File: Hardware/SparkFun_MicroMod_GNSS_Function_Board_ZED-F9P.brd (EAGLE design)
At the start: 37.5 x 65 mm, 160 parts, among them J1 USB Female Type C Connector, J10 U.FL, J11 455-1750-1-ND, J2 MICROMOD_FUNCTION_STANDARD, Q1 DMP21D0UT-7, U1 NLAST4501DFT2G, U10 SN74AUP1T04, U11 SN74AUP1T04, U2 3.3V, U3 EEPROM, U4 74LVC4066D_QUAD_BILATERAL_SWI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, U5 74LVC4066D_QUAD_BILATERAL_SWI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, U6 OPA344, U7 74LVC541A, U8 U-BLOX_ZED-F9P, U9 FIN1017MX

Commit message: Removed Acid Traps.
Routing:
- net ZED_DSEL: track 41.1 -> 41.5 mm, vias 6 -> 5
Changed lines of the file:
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@@
 <layer number="1" name="Top/Horz" color="4" fill="1" visible="yes" active="yes"/>
 <layer number="2" name="Route2" color="13" fill="3" visible="yes" active="yes"/>
-<layer number="15" name="Route15" color="47" fill="6" visible="yes" active="yes"/>
-<layer number="16" name="Bottom/Vert" color="9" fill="1" visible="yes" active="yes"/>
+<layer number="15" name="Route15" color="47" fill="6" visible="no" active="yes"/>
+<layer number="16" name="Bottom/Vert" color="9" fill="1" visible="no" active="yes"/>
 <layer number="17" name="Pads" color="2" fill="1" visible="yes" active="yes"/>
 <layer number="18" name="Vias" color="2" fill="1" visible="yes" active="yes"/>
-<layer number="19" name="Unrouted" color="6" fill="1" visible="yes" active="yes"/>
+<layer number="19" name="Unrouted" color="6" fill="1" visible="no" active="yes"/>
 <layer number="20" name="Dimension" color="24" fill="1" visible="yes" active="yes"/>
-<layer number="21" name="tPlace" color="16" fill="1" visible="yes" active="yes"/>
-<layer number="22" name="bPlace" color="14" fill="1" visible="yes" active="yes"/>
-<layer number="23" name="tOrigins" color="15" fill="1" visible="yes" active="yes"/>
-<layer number="24" name="bOrigins" color="15" fill="1" visible="yes" active="yes"/>
+<layer number="21" name="tPlace" color="16" fill="1" visible="no" active="yes"/>
+<layer number="22" name="bPlace" color="14" fill="1" visible="no" active="yes"/>
+<layer number="23" name="tOrigins" color="15" fill="1" visible="no" active="yes"/>
+<layer number="24" name="bOrigins" color="15" fill="1" visible="no" active="yes"/>
 <layer number="25" name="tNames" color="7" fill="1" visible="no" active="yes"/>
 <layer number="26" name="bNames" color="7" fill="1" visible="no" active="yes"/>
@@
 <layer number="37" name="tTest" color="7" fill="1" visible="no" active="yes"/>
 <layer number="38" name="bTest" color="7" fill="1" visible="no" active="yes"/>
-<layer number="39" name="tKeepout" color="4" fill="11" visible="yes" active="yes"/>
-<layer number="40" name="bKeepout" color="1" fill="11" visible="yes" active="yes"/>
-<layer number="41" name="tRestrict" color="4" fill="10" visible="yes" active="yes"/>
-<layer number="42" name="bRestrict" color="1" fill="10" visible="yes" active="yes"/>
+<layer number="39" name="tKeepout" color="4" fill="11" visible="no" active="yes"/>
+<layer number="40" name="bKeepout" color="1" fill="11" visible="no" active="yes"/>
+<layer number="41" name="tRestrict" color="4" fill="10" visible="no" active="yes"/>
+<layer number="42" name="bRestrict" color="1" fill="10" visible="no" active="yes"/>
 <layer number="43" name="vRestrict" color="2" fill="10" visible="no" active="yes"/>
 <layer number="44" name="Drills" color="7" fill="1" visible="no" active="yes"/>
-<layer number="45" name="Holes" color="7" fill="1" visible="yes" active="yes"/>
-<layer number="46" name="Milling" color="3" fill="1" visible="yes" active="yes"/>
-<layer number="47" name="Measures" color="7" fill="1" visible="yes" active="yes"/>
-<layer number="48" name="Document" color="7" fill="1" visible="yes" active="yes"/>
+<layer number="45" name="Holes" color="7" fill="1" visible="no" active="yes"/>
+<layer number="46" name="Milling" color="3" fill="1" visible="no" active="yes"/>
+<layer number="47" name="Measures" color="7" fill="1" visible="no" active="yes"/>
+<layer number="48" name="Document" color="7" fill="1" visible="no" active="yes"/>
 <layer number="49" name="Reference" color="7" fill="1" visible="no" active="yes"/>
 <layer number="50" name="dxf" color="7" fill="1" visible="no" active="yes"/>
-<layer number="51" name="tDocu" color="6" fill="1" visible="yes" active="yes"/>
-<layer number="52" name="bDocu" color="7" fill="1" visible="yes" active="yes"/>
+<layer number="51" name="tDocu" color="6" fill="1" visible="no" active="yes"/>
+<layer number="52" name="bDocu" color="7" fill="1" visible="no" active="yes"/>
 <layer number="91" name="Nets" color="2" fill="1" visible="no" active="no"/>
 <layer number="92" name="Busses" color="1" fill="1" visible="no" active="no"/>
@@
 <wire x1="17.865" y1="24.235" x2="16.695" y2="25.405" width="0.2" layer="2"/>
 <wire x1="17.865" y1="26.4" x2="17.865" y2="24.135" width="0.2" layer="1"/>
-<wire x1="20.405" y1="20.8" x2="20.405" y2="22.005" width="0.2" layer="1"/>
-<wire x1="21.675" y1="23.275" x2="20.405" y2="22.005" width="0.2" layer="2"/>
 <wire x1="21.675" y1="23.275" x2="21.7" y2="23.3" width="0.2" layer="2"/>
 <wire x1="21.675" y1="20.8" x2="21.675" y2="23.275" width="0.2" layer="1"/>
@@
 <via x="16.695" y="25.405" extent="1-16" drill="0.3"/>
 <via x="23.7" y="28.8" extent="1-16" drill="0.3"/>
-<via x="20.405" y="22.005" extent="1-16" drill="0.3"/>
 <via x="21.675" y="23.275" extent="1-16" drill="0.3"/>
 <wire x1="24.95" y1="42.2" x2="26.1" y2="42.2" width="0.11" layer="1"/>
@@
 <wire x1="24.4" y1="27.4" x2="23.7" y2="28.1" width="0.11" layer="16"/>
 <wire x1="23.7" y1="28.1" x2="23.7" y2="28.8" width="0.11" layer="16"/>
+<wire x1="20.405" y1="20.8" x2="20.405" y2="22.605" width="0.2" layer="1"/>
+<wire x1="20.405" y1="22.605" x2="21.1" y2="23.3" width="0.2" layer="1"/>
+<wire x1="21.1" y1="23.3" x2="21.65" y2="23.3" width="0.2" layer="1"/>
+<wire x1="21.65" y1="23.3" x2="21.675" y2="23.275" width="0.2" layer="1"/>
 </signal>
 <signal name="ZED_ANT_DETECT" class="11">
@@
 <contactref element="U5" pad="6"/>
 <contactref element="U5" pad="12"/>
-<wire x1="5.765" y1="24.135" x2="6.8" y2="23.1" width="0.2" layer="2"/>
+<wire x1="5.765" y1="24.135" x2="6.3" y2="23.6" width="0.2" layer="2"/>
 <wire x1="5.765" y1="24.135" x2="4.495" y2="25.405" width="0.2" layer="2"/>
 <wire x1="4.495" y1="25.405" x2="4.495" y2="26.4" width="0.2" layer="1"/>
@@
 <wire x1="16.05" y1="29.45" x2="15.95" y2="29.45" width="0.2" layer="15"/>
 <wire x1="15.95" y1="29.45" x2="9.6" y2="23.1" width="0.2" layer="15"/>
-<wire x1="6.8" y1="23.1" x2="9.6" y2="23.1" width="0.2" layer="2"/>
+<wire x1="9.1" y1="23.6" x2="6.3" y2="23.6" width="0.2" layer="2"/>
+<wire x1="9.1" y1="23.6" x2="9.6" y2="23.1" width="0.2" layer="2"/>
 <wire x1="9.6" y1="23.1" x2="9.6" y2="20.825" width="0.2" layer="1"/>
 <wire x1="9.6" y1="20.825" x2="9.575" y2="20.8" width="0.2" layer="1"/>

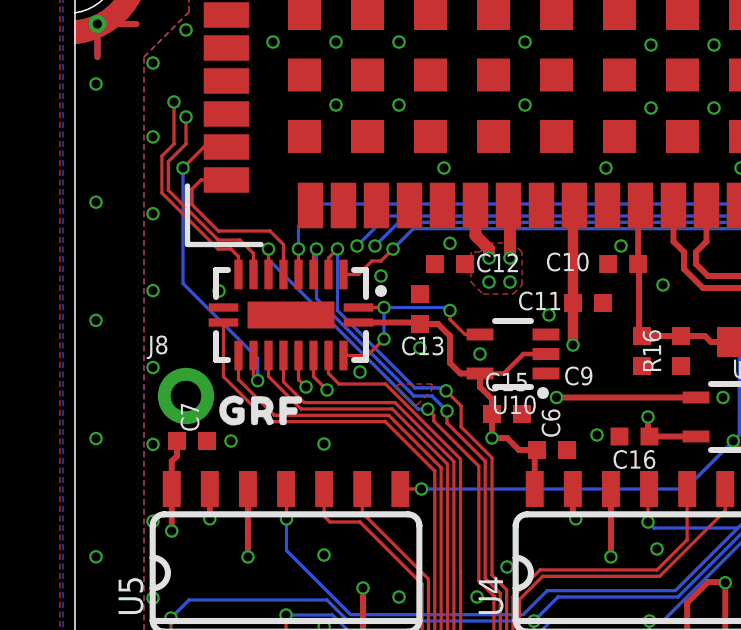
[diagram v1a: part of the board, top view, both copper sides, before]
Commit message: change due to mfgring issue.
There was no TSTOP on ground pad of U7. Added TSTOP.
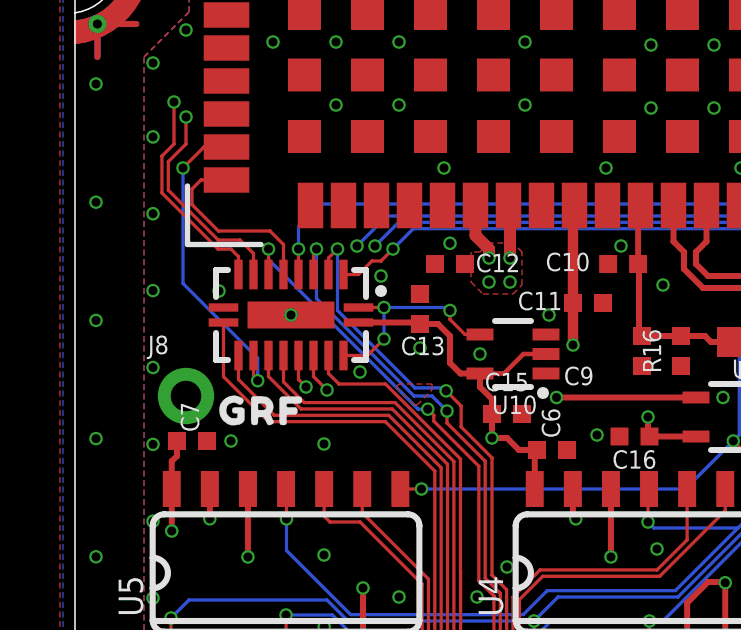
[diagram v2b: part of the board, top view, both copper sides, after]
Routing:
- net GND_RF: vias 158 -> 159
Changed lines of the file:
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@@
 <drawing>
 <settings>
-<setting alwaysvectorfont="no"/>
+<setting alwaysvectorfont="yes"/>
 <setting verticaltext="up"/>
 </settings>
@@
 <layer number="1" name="Top/Horz" color="4" fill="1" visible="yes" active="yes"/>
 <layer number="2" name="Route2" color="13" fill="3" visible="yes" active="yes"/>
-<layer number="15" name="Route15" color="47" fill="6" visible="no" active="yes"/>
-<layer number="16" name="Bottom/Vert" color="9" fill="1" visible="no" active="yes"/>
+<layer number="15" name="Route15" color="47" fill="6" visible="yes" active="yes"/>
+<layer number="16" name="Bottom/Vert" color="9" fill="1" visible="yes" active="yes"/>
 <layer number="17" name="Pads" color="2" fill="1" visible="yes" active="yes"/>
 <layer number="18" name="Vias" color="2" fill="1" visible="yes" active="yes"/>
 <layer number="19" name="Unrouted" color="6" fill="1" visible="no" active="yes"/>
 <layer number="20" name="Dimension" color="24" fill="1" visible="yes" active="yes"/>
-<layer number="21" name="tPlace" color="16" fill="1" visible="no" active="yes"/>
-<layer number="22" name="bPlace" color="14" fill="1" visible="no" active="yes"/>
-<layer number="23" name="tOrigins" color="15" fill="1" visible="no" active="yes"/>
+<layer number="21" name="tPlace" color="16" fill="1" visible="yes" active="yes"/>
+<layer number="22" name="bPlace" color="14" fill="1" visible="yes" active="yes"/>
+<layer number="23" name="tOrigins" color="15" fill="1" visible="yes" active="yes"/>
 <layer number="24" name="bOrigins" color="15" fill="1" visible="no" active="yes"/>
 <layer number="25" name="tNames" color="7" fill="1" visible="no" active="yes"/>
@@
 <layer number="27" name="tValues" color="7" fill="1" visible="no" active="yes"/>
 <layer number="28" name="bValues" color="7" fill="1" visible="no" active="yes"/>
-<layer number="29" name="tStop" color="7" fill="3" visible="no" active="yes"/>
+<layer number="29" name="tStop" color="7" fill="3" visible="yes" active="yes"/>
 <layer number="30" name="bStop" color="7" fill="6" visible="no" active="yes"/>
-<layer number="31" name="tCream" color="7" fill="4" visible="no" active="yes"/>
+<layer number="31" name="tCream" color="7" fill="4" visible="yes" active="yes"/>
 <layer number="32" name="bCream" color="7" fill="5" visible="no" active="yes"/>
 <layer number="33" name="tFinish" color="6" fill="3" visible="no" active="yes"/>
@@
 </element>
 <element name="U1" library="SparkFun_MicroMod_GNSS_Function_Board_ZED-F9P" package="SOT353" value="NLAST4501DFT2G" x="26.4" y="31.3" smashed="yes" rot="R270">
-<attribute name="PROD_ID" value="NA" x="26.4" y="31.3" size="1.778" layer="27" rot="R270" display="off"/>
+<attribute name="PROD_ID" value="IC-16759" x="26.4" y="31.3" size="1.778" layer="27" rot="R270" display="off"/>
 <attribute name="VALUE" value="NLAST4501DFT2G" x="26.4" y="31.3" size="1.778" layer="27" rot="R270" display="off"/>
 </element>
@@
 </polygon>
 <contactref element="JP8" pad="1"/>
+<via x="7.2" y="32.2" extent="1-16" drill="0.3"/>
 </signal>
 <signal name="RF_IN" class="3">

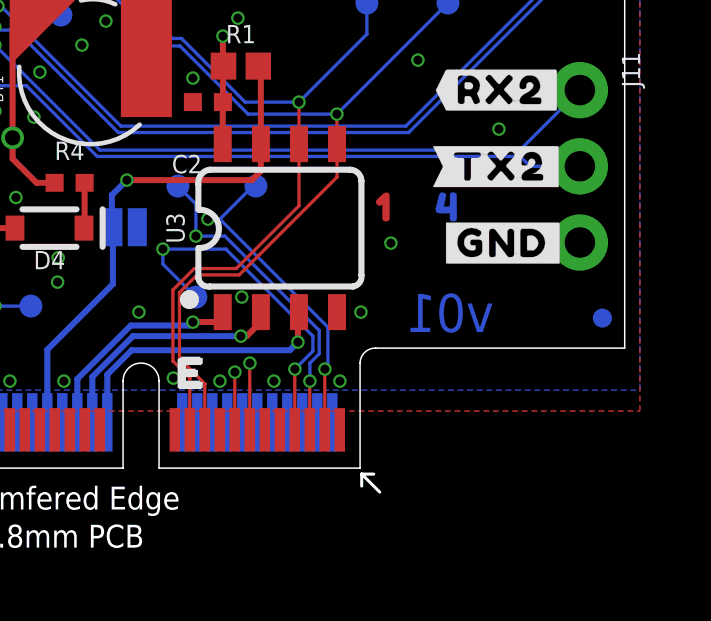
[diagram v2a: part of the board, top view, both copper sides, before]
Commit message: update to v02 for mfgr error.
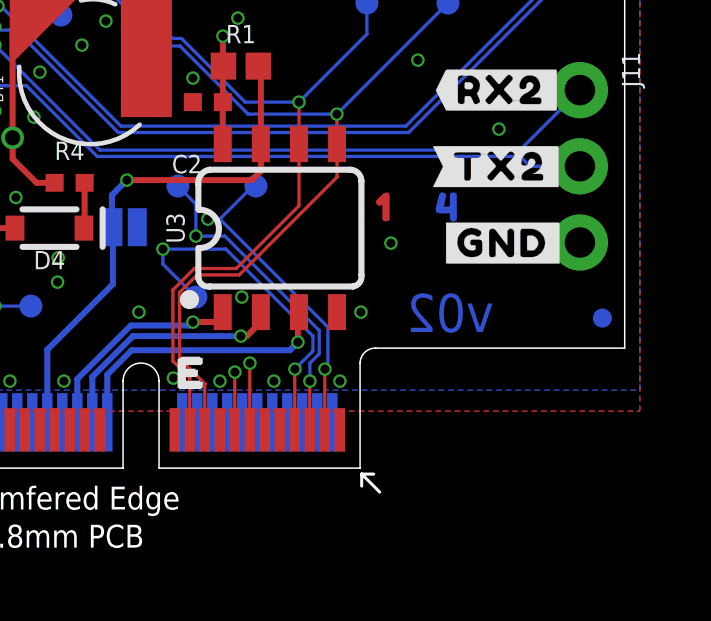
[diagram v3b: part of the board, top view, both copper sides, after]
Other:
- board text added: "v02"
- board text removed: "v01"
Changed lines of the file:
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@@
 <drawing>
 <settings>
-<setting alwaysvectorfont="yes"/>
+<setting alwaysvectorfont="no"/>
 <setting verticaltext="up"/>
 </settings>
@@
 <plain>
 <wire x1="28.672" y1="0" x2="21.972" y2="0" width="0.05" layer="20"/>
-<text x="31.67" y="5.17" size="1.27" layer="16" font="vector" ratio="20" rot="SMR0" align="center">v01</text>
+<text x="31.67" y="5.17" size="1.27" layer="16" font="vector" ratio="20" rot="SMR0" align="center">v02</text>
 <text x="62.23" y="-8.89" size="1.778" layer="51" font="vector">A. Brudner</text>
 <wire x1="20.772" y1="0" x2="8.822" y2="0" width="0.05" layer="20"/>

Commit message: v03 protos update.
Center and update flags.
Fix RTK STAT circuit.
Fix voltage divider for USB detect.
Add I2C PURs.
Add a PUR for the reset line outside isolation.
Changed PWR LED resistor to 1k.
Moved PPS and RTK LEDs to top of board.
Removed RF_GND.
Rerouted board.
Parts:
- removed J17: (no value), SparkFun-Connectors:1X04_NO_SILK
- removed SUPPLYTIE1: 2PT_GND_TIE, SparkFun-PowerSymbols:2PT_GND_TIE
- removed U$105: (no value), output:##RESET##0
- removed U$38: (no value), output:43213
- removed U$39: (no value), output:#RTCMTX#0
- removed U$40: (no value), output:#RTCMRX#0
- removed U$41, U$42, U$43, U$57, U$58, U$59, U$78, U$79, U$83, U$99: (no value), output:#GND#0
- removed U$53: (no value), output:#RTK#2255
- removed U$55, U$67: (no value), output:#GRF#0
- removed U$56: (no value), output:G2
- removed U$60: (no value), output:#EXTINT#0
- removed U$61: (no value), output:#EXTINT#2
- removed U$65: (no value), output:##RESET##3
- removed U$66: (no value), output:#I�C#SER#0
- removed U$70: (no value), output:#SPI#30
- removed U$75: (no value), output:#PWR0
- removed U$77: (no value), output:#SUP#0
- removed U$95: (no value), output:#DSEL#31
- removed U$97: (no value), output:#RX2#2249
- removed U$98: (no value), output:#TX2#2249
- added J3: (no value), SparkFun-Connectors:1X01_NO_SILK
- added JP9: JUMPER-SMT_3_1-NC_TRACE_SILK, SparkFun-Jumpers:SMT-JUMPER_3_1-NC_TRACE_SILK
- added R19: 47k, SparkFun-Resistors:0402-TIGHT
- added R20, R21: 10k, SparkFun-Resistors:0402-TIGHT
- added U$1: (no value), output:40
- added U$10, U$11, U$18, U$19, U$21, U$22, U$25, U$33, U$5, U$6, U$7, U$9: (no value), output:#_GND_#0
- added U$12: (no value), output:#_RTCMRX#0
- added U$13: (no value), output:#RX2_#0
- added U$14: (no value), output:##RESET_##0
- added U$15: (no value), output:#_#RESET##0
- added U$16: (no value), output:#_EXTINT#0
- added U$17: (no value), output:#EXTINT_#0
- added U$2: (no value), output:#_RTCMTX#0
- added U$23: (no value), output:#_I�C#SER#0
- added U$24: (no value), output:#SPI_#0
- added U$28: (no value), output:#_I�C#0
- added U$29: (no value), output:#_DSEL#0
- added U$3: (no value), output:#TX2_#0
- added U$30: (no value), output:#SUP#0
- added U$31: (no value), output:#RTK#0
- added U$32: (no value), output:#PWR#0
- D4: value 0.5A/40V/420mV -> RED; device SparkFun-DiscreteSemi:SOD-323 -> SparkFun-LED:LED-0603
- D5: value RED -> BLUE
- D7: value BLUE -> 0.5A/40V/420mV; device SparkFun-LED:LED-0603 -> SparkFun-DiscreteSemi:SOD-323
- J10: value U.FL -> 455-1750-1-ND; device SparkFun-Connectors:U.FL -> SparkFun-Connectors:1X03_NO_SILK
- J11: value 455-1750-1-ND -> (none); device SparkFun-Connectors:1X03_NO_SILK -> SparkFun-Connectors:1X01_NO_SILK
- J12: device SparkFun-Connectors:1X01_NO_SILK -> SparkFun-Connectors:1X02_NO_SILK
- J14: device SparkFun-Connectors:1X02_NO_SILK -> SparkFun-Connectors:1X04_NO_SILK
- J6: device SparkFun-Connectors:1X01_NO_SILK -> SparkFun-Connectors:1X01_SMALL
- J7: device SparkFun-Connectors:1X01_SMALL -> SparkFun-Connectors:1X01_NO_SILK
- J9: value (none) -> U.FL; device SparkFun-Connectors:1X01_NO_SILK -> SparkFun-Connectors:U.FL
- JP7: value JUMPER-SMT_3_1-NC_TRACE_SILK -> JUMPER-SMT_3_2-NC_TRACE_SILK; device SparkFun-Jumpers:SMT-JUMPER_3_1-NC_TRACE_SILK -> SparkFun-Jumpers:SMT-JUMPER_3_2-NC_TRACE_SILK
- R1: device SparkFun-Resistors:0402 -> SparkFun-Resistors:0402-TIGHT
- R10: value 10k -> 27; device SparkFun-Resistors:0402 -> SparkFun-Resistors:0402-TIGHT
- R11: value 10k -> 2.2k; device SparkFun-Resistors:0402 -> SparkFun-Resistors:0402-TIGHT
- R12: value 100k -> 2.2k
- R13: value 100k -> 10k
- R14: value 10 -> 10k; device SparkFun-Resistors:0603 -> SparkFun-Resistors:0402-TIGHT
- R15: value 68.1k -> 1k; device SparkFun-Resistors:0603 -> SparkFun-Resistors:0402-TIGHT
- R17: value 10k -> 10; device SparkFun-Resistors:0402 -> SparkFun-Resistors:0603
- R18: value 10k -> 22k; device SparkFun-Resistors:0402 -> SparkFun-Resistors:0402-TIGHT
- R2: value 5.1k -> 10k
- R4: value 3.3K -> 5.1k
- R5: value 27 -> 3.3K
- R6: value 27 -> 1k
- R7: value 100k -> 1k
- R8: value 1KOHM-0402-1/16W-1% -> 1k; device SparkFun-Resistors:0402 -> SparkFun-Resistors:0402-TIGHT
- R9: value 1KOHM-0402-1/16W-1% -> 27; device SparkFun-Resistors:0402 -> SparkFun-Resistors:0402-TIGHT
- moved U$51 58.8 mm to (0.60, 64.0)
- moved U$52 58.8 mm to (4.40, 64.0)
- moved JP6 56.7 mm to (2.50, 61.8)
- moved JP5 56.3 mm to (6.50, 61.8)
- moved U$50 55.5 mm to (2.50, 60.9), turned to 270 degrees
- moved D4 54.3 mm to (10.5, 61.7), turned to 270 degrees
- moved D6 54.2 mm to (2.50, 61.7)
- moved R8 53.8 mm to (4.50, 61.4)
- moved R2 53.1 mm to (13.9, 6.10)
- moved R9 51.7 mm to (29.2, 55.1)
- moved R4 50.2 mm to (33.4, 57.6), turned to 180 degrees
- moved J10 49.4 mm to (36.0, 12.6)
- moved R5 46.7 mm to (19.0, 9.51), turned to 0 degrees
- moved R11 45.4 mm to (26.6, 13.9), turned to 90 degrees
- moved R12 44.5 mm to (27.9, 13.9)
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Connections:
- removed net GND_RF: C10.2, C11.2, C12.2, C13.2, C15.2, C16.2, C4.2, C5.2, C6.2, C7.2, C9.2, D8.2, J10.1, J10.2, J8.1, J9.1, JP4.2, JP8.1, R11.1, R13.1, R16.1, SUPPLYTIE1.P$1, U1.3, U10.3, U11.3, U4.7, U5.7, U6.2, U7.10, U7.EPAD, U8.1, U8.100, U8.101, U8.102, U8.12, U8.14, U8.3, U8.32, U8.37, U8.41, U8.48, U8.55, U8.56, U8.57, U8.58, U8.59, U8.60, U8.61, U8.62, U8.63, U8.64, U8.65, U8.66, U8.67, U8.68, U8.69, U8.70, U8.71, U8.72, U8.73, U8.74, U8.75, U8.76, U8.77, U8.78, U8.79, U8.80, U8.81, U8.82, U8.83, U8.84, U8.85, U8.86, U8.87, U8.88, U8.89, U8.90, U8.91, U8.92, U8.93, U8.94, U8.95, U8.96, U8.97, U8.98, U8.99
- removed net N$29 (its old number): D7.C, R9.2
- new net N$2: JP8.3, R14.2
- new net N$30: D4.C, R6.2
- new net N$9: JP7.1, R12.2
- net !RESET!: now also J12.1, R20.2; no longer J13.1
- net 3.3V: now also D7.A; no longer D4.A
- net 5V: now also R2.1; no longer R18.1
- net EXTINT: now also J13.1; no longer J14.1
- net GND: now also C10.2, C11.2, C12.2, C13.2, C15.2, C16.2, C4.2, C5.2, C6.2, C7.2, C9.2, D8.2, J10.3, J12.2, J14.1, J14.4, J4.1, J7.1, J8.1, J9.1, J9.2, JP4.2, JP9.1, R14.1, R16.1, R19.1, R4.1, U1.3, U10.3, U11.3, U4.7, U5.7, U6.2, U7.10, U7.EPAD, U8.1, U8.100, U8.101, U8.102, U8.12, U8.14, U8.3, U8.32, U8.37, U8.41, U8.48, U8.55, U8.56, U8.57, U8.58, U8.59, U8.60, U8.61, U8.62, U8.63, U8.64, U8.65, U8.66, U8.67, U8.68, U8.69, U8.70, U8.71, U8.72, U8.73, U8.74, U8.75, U8.76, U8.77, U8.78, U8.79, U8.80, U8.81, U8.82, U8.83, U8.84, U8.85, U8.86, U8.87, U8.88, U8.89, U8.90, U8.91, U8.92, U8.93, U8.94, U8.95, U8.96, U8.97, U8.98, U8.99; no longer J11.3, J14.2, J17.1, J17.4, J6.1, JP5.1, R2.1, SUPPLYTIE1.P$2
- net MM_SCL: now also R11.1
- net MM_SDA: now also R12.1
- net N$1: now also JP8.1, R13.1; no longer JP7.1, R10.1
- net N$13: now also R15.1, R17.1; no longer R12.1, R14.1
- net N$14: now also R18.2, R19.2; no longer R15.2, R16.2
- net N$26: now also R6.1; no longer R7.1
- net N$27: now also JP6.2; no longer JP5.2
- net N$3: now also R3.2; no longer R2.2
- net N$32: now also D7.C, R5.2; no longer D4.C, R4.2
- net N$4: now also R4.2; no longer R3.2
- net N$48: now also R15.2, R16.2; no longer R12.2, R13.2
- net N$5: now also JP9.3, R21.1; no longer JP8.3, R17.1
- net N$7: now also J9.FEED; no longer J10.FEED
- net N$8: now also JP5.2, R7.1; no longer JP6.2, R9.1
- net PPS: no longer D6.A
- net PPS_DIFF_N: now also J14.3; no longer J17.3
- net PPS_DIFF_P: now also J14.2; no longer J17.2
- net PWR_EN: now also R2.2; no longer R18.2
- net RTK_STAT: no longer D7.A
- net RX2/RTCM: now also J10.1; no longer J11.1
- net TX2/RTCM: now also J10.2; no longer J11.2
- net USB_N: now also R10.1; no longer R6.1
- net USB_P: now also R9.1; no longer R5.1
- net V_BATT: now also J6.P$1, R5.1; no longer J7.P$1, R4.1
- net V_RF: now also R13.2; no longer R10.2
- net V_ZED: now also D4.A, J3.1, JP7.2, R20.1, R21.2; no longer J4.1, R17.2
- net ZED_!SAFEBOOT!: now also J11.1; no longer J12.1
- net ZED_ANT_!SHORT!: now also R17.2; no longer R14.2
- net ZED_ANT_OFF: now also JP8.2; no longer JP7.2
- net ZED_DSEL: now also JP9.2; no longer JP8.2
- net ZED_PPS: now also D6.A
- net ZED_RTK_STAT: now also JP5.1
- net ZED_USB_DET: now also R18.1; no longer R15.1
- net ZED_USB_N: now also R10.2; no longer R6.2
- net ZED_USB_P: now also R9.2; no longer R5.2
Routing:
- net ZED_PPS: track 32.3 -> 73.6 mm, vias 2 -> 3
- net ZED_RTK_STAT: track 14.9 -> 32.4 mm, vias 2 -> 1
- net !RESET!: track 78.6 -> 88.4 mm
- net PPS: track 44.9 -> 37.7 mm
- net MM_!CS!: track 32.8 -> 26.1 mm
- net V_ZED: track 29.9 -> 36.2 mm
- net GND_RF: track 6.34 -> 0.00 mm, vias 159 -> 0
- net N$9: track 0.00 -> 5.70 mm, vias 0 -> 1
- net MM_SCK: track 46.4 -> 40.9 mm
- net GND: track 6.51 -> 1.44 mm, vias 96 -> 167
- net V_RF: track 9.87 -> 5.48 mm
- net N$27: track 6.49 -> 3.01 mm
- net ZED_ANT_OFF: track 13.6 -> 10.2 mm, vias 2 -> 1
- net MM_SCL: track 36.0 -> 32.6 mm
- net ZED_ANT_!SHORT!: track 13.7 -> 10.4 mm
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- removed copper zone on layer 15, net GND
- removed copper zone on layer 1, net GND_RF
- removed copper zone on layer 16, net GND_RF
- removed copper zone on layer 2, net GND_RF
- removed copper zone on layer 2, net V_ZED
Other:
- board text added: "v03"
- board text removed: "v02"
